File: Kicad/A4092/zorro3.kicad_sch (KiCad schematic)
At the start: 13 parts, among them CN1 Zorro3, U1 SN74ABT16543DGGR, U2 SN74ABT16543DGGR, U3 SN74ABT16543DGGR, U4 SN74ABT16543DGGR, U5 74LVC07APW_118, U6 SN74ABT16245ADGGR

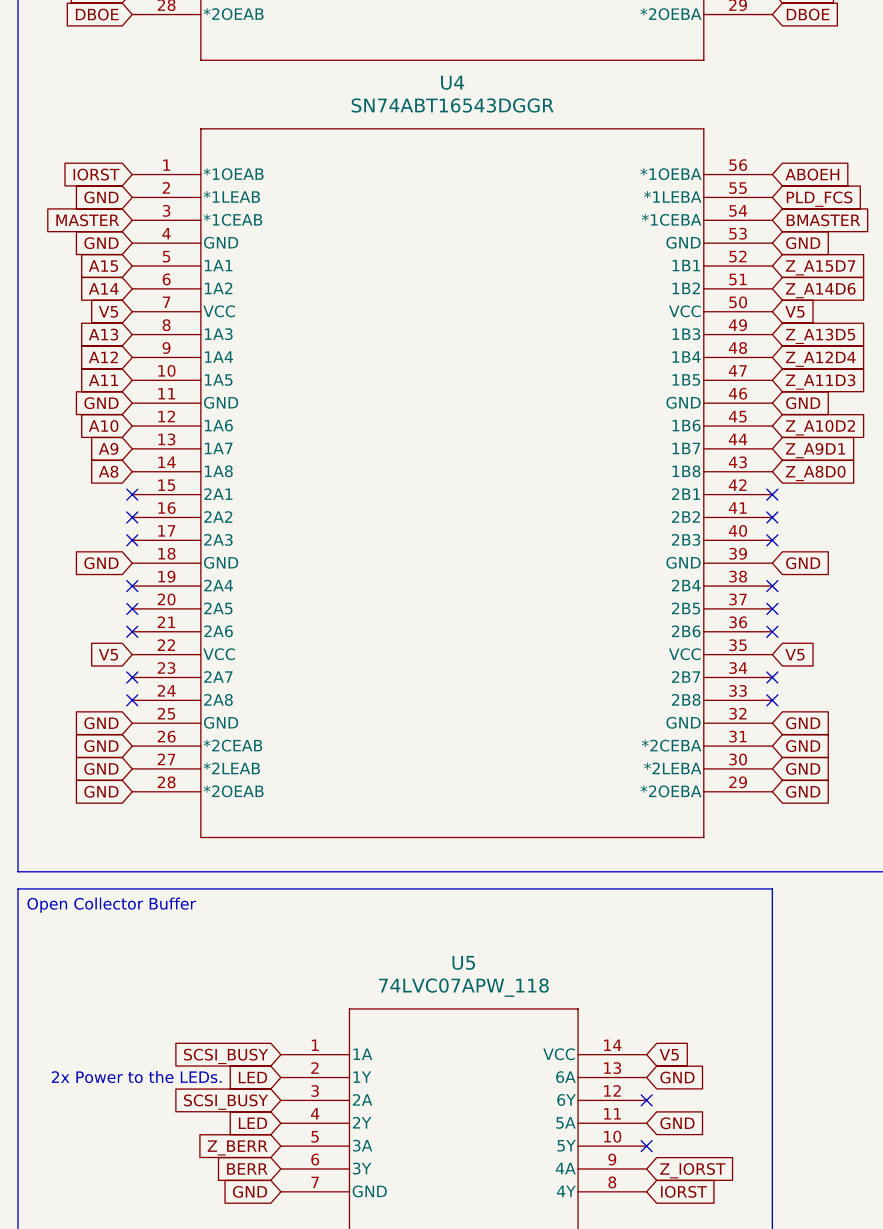
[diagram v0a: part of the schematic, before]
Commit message: Update Schematics and PCB with fixes for known issues
This commit fixes:
* U4 enable IORST -> ABOEH
* U5 VCC 5V -> 3.3V
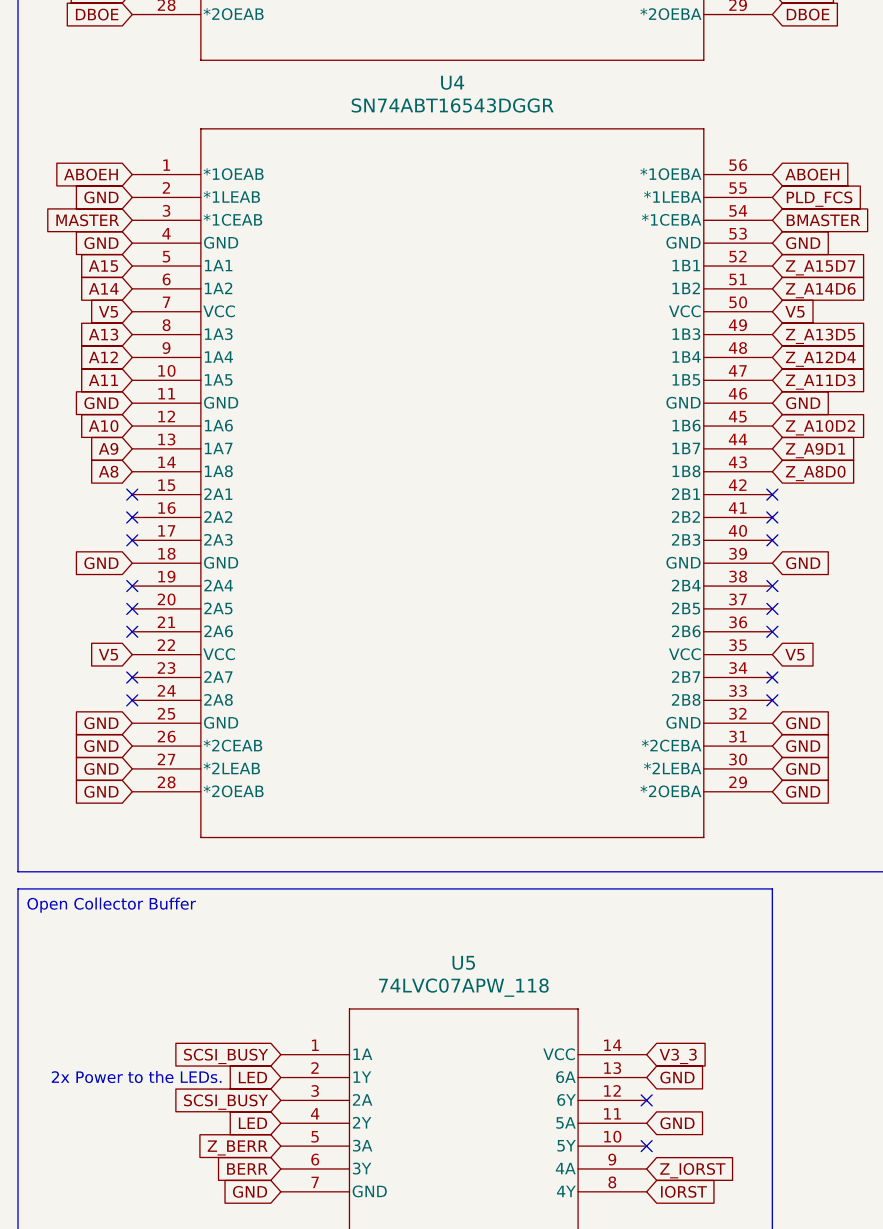
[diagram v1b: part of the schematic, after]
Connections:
- net ABOEH: now also U4.1 (*1OEAB)
- net IORST: no longer U4.1 (*1OEAB)
- net V5: no longer U5.14 (VCC)
- new net V3_3: U5.14 (VCC)
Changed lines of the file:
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@@
 		)
 	)
+	(global_label "ABOEH"
+		(shape input)
+		(at 27.94 118.11 180)
+		(fields_autoplaced yes)
+		(effects
+			(font
+				(size 1.27 1.27)
+			)
+			(justify right)
+		)
+		(property "Intersheetrefs" "${INTERSHEET_REFS}"
+			(at 18.7862 118.11 0)
+			(effects
+				(font
+					(size 1.27 1.27)
+				)
+				(justify right)
+				(hide yes)
+			)
+		)
+	)
 	(global_label "BMASTER"
 		(shape input)
@@
 		)
 	)
-	(global_label "V5"
-		(shape input)
-		(at 85.09 215.9 0)
-		(fields_autoplaced yes)
-		(effects
-			(font
-				(size 1.27 1.27)
-			)
-			(justify left)
-		)
-		(property "Intersheetrefs" "${INTERSHEET_REFS}"
-			(at 90.3733 215.9 0)
-			(effects
-				(font
-					(size 1.27 1.27)
-				)
-				(justify left)
-				(hide yes)
-			)
-		)
-	)
 	(global_label "D8"
 		(shape input)
@@
 		)
 	)
-	(global_label "IORST"
-		(shape input)
-		(at 27.94 118.11 180)
-		(fields_autoplaced yes)
-		(effects
-			(font
-				(size 1.27 1.27)
-			)
-			(justify right)
-		)
-		(property "Intersheetrefs" "${INTERSHEET_REFS}"
-			(at 19.5724 118.11 0)
-			(effects
-				(font
-					(size 1.27 1.27)
-				)
-				(justify right)
-				(hide yes)
-			)
-		)
-	)
 	(global_label "GND"
 		(shape input)
@@
 			(effects
 				(font
+					(size 1.27 1.27)
+				)
+				(justify left)
+				(hide yes)
+			)
+		)
+	)
+	(global_label "V3_3"
+		(shape input)
+		(at 85.09 215.9 0)
+		(fields_autoplaced yes)
+		(effects
+			(font
+				(size 1.27 1.27)
+			)
+			(justify left)
+		)
+		(property "Intersheetrefs" "${INTERSHEET_REFS}"
+			(at 92.5504 215.9 0)
+			(effects
+				(font
